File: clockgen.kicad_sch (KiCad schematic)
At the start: 146 parts, among them IC3 TLV74325PDBVR, J13 73391-0083, J14 73391-0083, J15 292161-3, J16 U.FL-R-SMT-180, Q10 BSS138, Q9 BSS138, U12 AZ1117-3.3, U13 AZ1117-3.3, U14 TCA6416APWR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

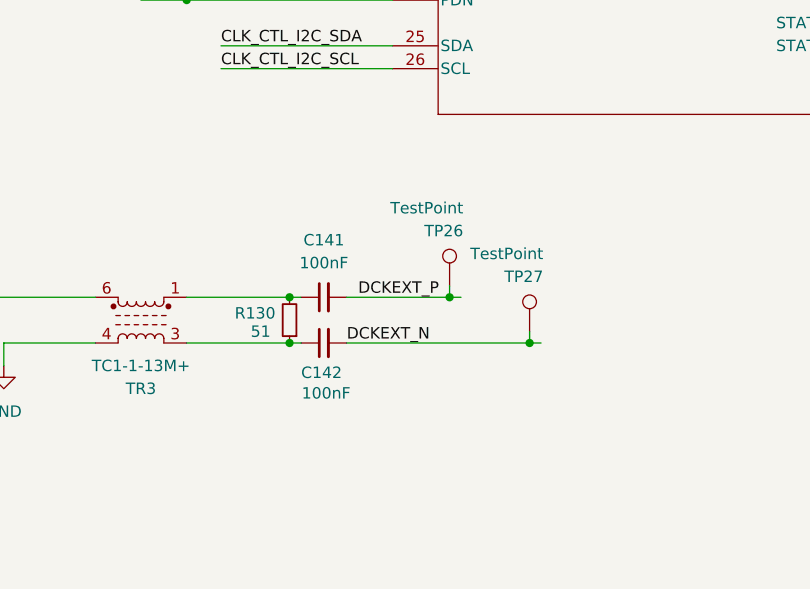
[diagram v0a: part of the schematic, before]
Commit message: schema: external clock input redone
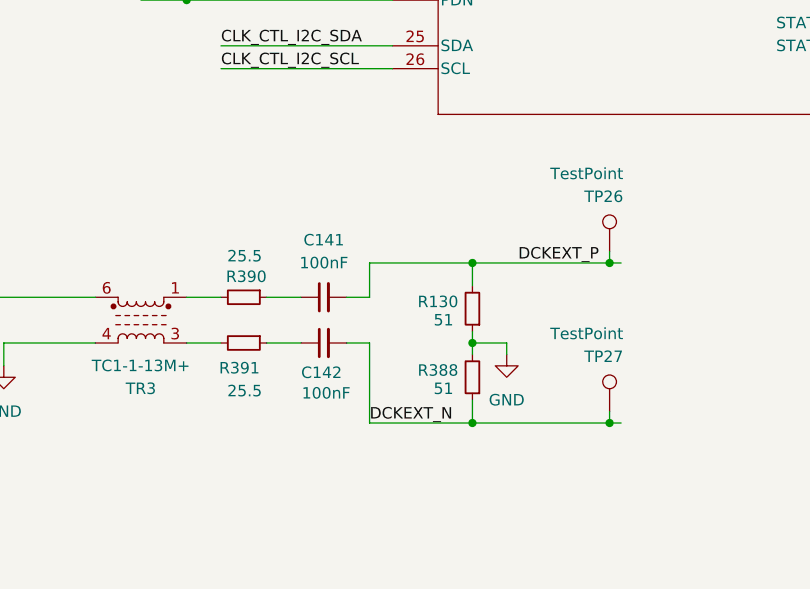
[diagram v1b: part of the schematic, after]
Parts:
- added R388: 51, Resistor_SMD:R_0402_1005Metric, symbol Device:R_Small
- added R390, R391: 25.5, Resistor_SMD:R_0402_1005Metric, symbol Device:R_Small
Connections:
- net DCKEXT_N: now also R388.1
- net DCKEXT_P: now also R130.2
- net GND: now also R130.1, R388.2
- new net: C142.1, R391.1
- new net: R390.2, TR3.1
- new net: R391.2, TR3.3
- new net: C141.1, R390.1
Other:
- moved on the sheet: R130, TP26, TP27

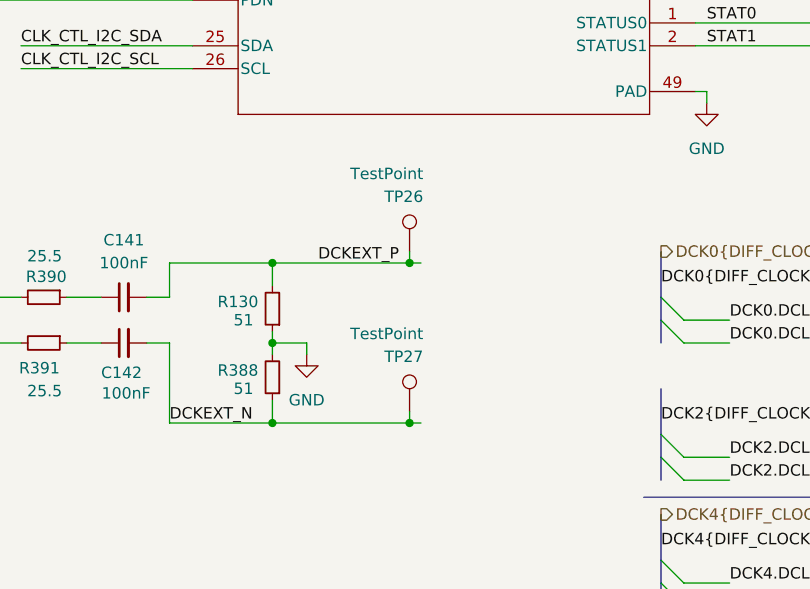
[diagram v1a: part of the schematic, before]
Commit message: ext clock input change
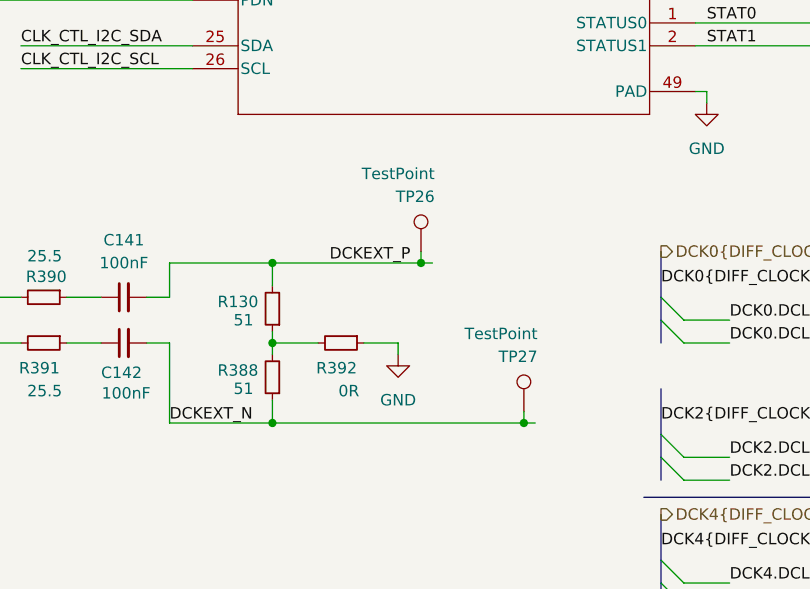
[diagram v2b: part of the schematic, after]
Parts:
- added R392: 0R, Resistor_SMD:R_0603_1608Metric, symbol Device:R_Small
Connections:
- net GND: now also R392.1; no longer R130.1, R388.2
- new net: R130.1, R388.2, R392.2
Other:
- moved on the sheet: TP26, TP27
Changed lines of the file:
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@@
 	(title_block
 		(title "NASR-M")
-		(date "2025-10-21")
-		(rev "D 0.9.4")
+		(date "2025-10-22")
+		(rev "D 0.9.5")
 		(company "electrodyssey.net")
 		(comment 1 "Onboard clock generator with optional external synchronization")
@@
 	)
 	(junction
-		(at 313.69 215.9)
+		(at 326.39 215.9)
 		(diameter 0)
 		(color 0 0 0 0)
@@
 	)
 	(junction
-		(at 313.69 198.12)
+		(at 314.96 198.12)
 		(diameter 0)
 		(color 0 0 0 0)
@@
 	(wire
 		(pts
-			(xy 298.45 215.9) (xy 313.69 215.9)
-		)
-		(stroke
-			(width 0)
-			(type default)
-		)
-	)
-	(wire
-		(pts
 			(xy 38.1 38.1) (xy 49.53 38.1)
 		)
@@
 	(wire
 		(pts
-			(xy 302.26 208.28) (xy 302.26 207.01)
-		)
-		(stroke
-			(width 0)
-			(type default)
-		)
-	)
-	(wire
-		(pts
 			(xy 314.96 43.18) (xy 314.96 41.91)
 		)
@@
 	(wire
 		(pts
-			(xy 313.69 215.9) (xy 314.96 215.9)
+			(xy 326.39 215.9) (xy 327.66 215.9)
 		)
 		(stroke
@@
 	(wire
 		(pts
+			(xy 298.45 215.9) (xy 326.39 215.9)
+		)
+		(stroke
+			(width 0)
+			(type default)
+		)
+	)
+	(wire
+		(pts
 			(xy 193.04 199.39) (xy 195.58 199.39)
 		)
@@
 	(wire
 		(pts
+			(xy 298.45 198.12) (xy 314.96 198.12)
+		)
+		(stroke
+			(width 0)
+			(type default)
+		)
+	)
+	(wire
+		(pts
 			(xy 182.88 240.03) (xy 193.04 240.03)
 		)
@@
 	(wire
 		(pts
-			(xy 313.69 196.85) (xy 313.69 198.12)
+			(xy 314.96 196.85) (xy 314.96 198.12)
 		)
 		(stroke
@@
 	(wire
 		(pts
-			(xy 313.69 198.12) (xy 314.96 198.12)
+			(xy 314.96 198.12) (xy 316.23 198.12)
 		)
 		(stroke
@@
 	(wire
 		(pts
+			(xy 308.61 207.01) (xy 312.42 207.01)
+		)
+		(stroke
+			(width 0)
+			(type default)
+		)
+	)
+	(wire
+		(pts
 			(xy 259.08 73.66) (xy 259.08 72.39)
 		)
@@
 	(wire
 		(pts
-			(xy 302.26 207.01) (xy 298.45 207.01)
+			(xy 298.45 207.01) (xy 303.53 207.01)
 		)
 		(stroke
@@
 	(wire
 		(pts
-			(xy 298.45 198.12) (xy 313.69 198.12)
-		)
-		(stroke
-			(width 0)
-			(type default)
-		)
-	)
-	(wire
-		(pts
 			(xy 212.09 266.7) (xy 212.09 267.97)
 		)
@@
 	(wire
 		(pts
-			(xy 313.69 214.63) (xy 313.69 215.9)
+			(xy 326.39 214.63) (xy 326.39 215.9)
 		)
 		(stroke
@@
 	(wire
 		(pts
+			(xy 312.42 208.28) (xy 312.42 207.01)
+		)
+		(stroke
+			(width 0)
+			(type default)
+		)
+	)
+	(wire
+		(pts
 			(xy 201.93 261.62) (xy 201.93 267.97)
 		)
@@
 	)
 	(label "DCKEXT_P"
-		(at 303.53 198.12 0)
+		(at 304.8 198.12 0)
 		(effects
 			(font
@@
 	(symbol
 		(lib_id "Connector:TestPoint")
-		(at 313.69 196.85 0)
+		(at 314.96 196.85 0)
 		(unit 1)
 		(exclude_from_sim no)
@@
 		(dnp no)
 		(property "Reference" "TP26"
-			(at 315.214 190.754 0)
+			(at 316.484 190.754 0)
 			(effects
 				(font
@@
 		)
 		(property "Value" "TestPoint"
-			(at 315.214 188.214 0)
+			(at 316.484 188.214 0)
 			(effects
 				(font
@@
 		)
 		(property "Footprint" "TestPoint:TestPoint_Pad_D1.0mm"
-			(at 318.77 196.85 0)
+			(at 320.04 196.85 0)
 			(effects
 				(font
@@
 		)
 		(property "Datasheet" "~"
-			(at 318.77 196.85 0)
+			(at 320.04 196.85 0)
 			(effects
 				(font
@@
 		)
 		(property "Description" "test point"
-			(at 313.69 196.85 0)
+			(at 314.96 196.85 0)
 			(effects
 				(font
@@
 		)
 		(property "Mouser " ""
-			(at 313.69 196.85 0)
+			(at 314.96 196.85 0)
 			(effects
 				(font
@@
 	(symbol
 		(lib_id "power:GND")
-		(at 302.26 208.28 0)
+		(at 312.42 208.28 0)
 		(unit 1)
 		(exclude_from_sim no)
@@
 		(fields_autoplaced yes)
 		(property "Reference" "#PWR060"
-			(at 302.26 214.63 0)
+			(at 312.42 214.63 0)
 			(effects
 				(font
@@
 		)
 		(property "Value" "GND"
-			(at 302.26 213.36 0)
+			(at 312.42 213.36 0)
 			(effects
 				(font
@@
 		)
 		(property "Footprint" ""
-			(at 302.26 208.28 0)
+			(at 312.42 208.28 0)
 			(effects
 				(font
@@
 		)
 		(property "Datasheet" ""
-			(at 302.26 208.28 0)
+			(at 312.42 208.28 0)
 			(effects
 				(font
@@
 		)
 		(property "Description" "Power symbol creates a global label with name \"GND\" , ground"
-			(at 302.26 208.28 0)
+			(at 312.42 208.28 0)
 			(effects
 				(font
@@
 	)
 	(symbol
+		(lib_id "Device:R_Small")
+		(at 306.07 207.01 270)
+		(unit 1)
+		(exclude_from_sim no)
+		(in_bom yes)
+		(on_board yes)
+		(dnp no)
+		(property "Reference" "R392"
+			(at 307.848 209.804 90)
+			(effects
+				(font
+					(size 1.27 1.27)
+				)
+				(justify right)
+			)
+		)
+		(property "Value" "0R"
+			(at 308.102 212.344 90)
+			(effects
+				(font
+					(size 1.27 1.27)
+				)
+				(justify right)
+			)
+		)
+		(property "Footprint" "Resistor_SMD:R_0603_1608Metric"
+			(at 306.07 207.01 0)
+			(effects
+				(font
+					(size 1.27 1.27)
+				)
+				(hide yes)
+			)
+		)
+		(property "Datasheet" "~"
+			(at 306.07 207.01 0)
+			(effects
+				(font
+					(size 1.27 1.27)
+				)
+				(hide yes)
+			)
+		)
+		(property "Description" ""
+			(at 306.07 207.01 0)
+			(effects
+				(font
+					(size 1.27 1.27)
+				)
+				(hide yes)
+			)
+		)
+		(property "JLCPCB Part #" "C2906974"
+			(at 306.07 207.01 0)
+			(effects
+				(font
+					(size 1.27 1.27)
+				)
+				(hide yes)
+			)
+		)
+		(property "Part" "FRC0603F0000TS"
+			(at 306.07 207.01 90)
+			(effects
+				(font
+					(size 1.27 1.27)
+				)
+				(hide yes)
+			)
+		)
+		(property "Mouser " ""
+			(at 306.07 207.01 90)
+			(effects
+				(font
+					(size 1.27 1.27)
+				)
+				(hide yes)
+			)
+		)
+		(pin "1"
+		)
+		(pin "2"
+		)
+		(instances
+			(project "NASR"
+				(path "/9a13c8f9-b8a2-41aa-b5bd-813f44236e01/9e585404-97af-4e2a-aa37-2875da9a13db"
+					(reference "R392")
+					(unit 1)
+				)
+			)
+		)
+	)
+	(symbol
 		(lib_id "Device:C_Small")
 		(at 252.73 104.14 180)
@@
 	(symbol
 		(lib_id "Connector:TestPoint")
-		(at 313.69 214.63 0)
+		(at 326.39 214.63 0)
 		(unit 1)
 		(exclude_from_sim no)
@@
 		(dnp no)
 		(property "Reference" "TP27"
-			(at 315.214 208.534 0)
+			(at 327.914 208.534 0)
 			(effects
 				(font
@@
 		)
 		(property "Value" "TestPoint"
-			(at 315.214 205.994 0)
+			(at 327.914 205.994 0)
 			(effects
 				(font
@@
 		)
 		(property "Footprint" "TestPoint:TestPoint_Pad_D1.0mm"
-			(at 318.77 214.63 0)
+			(at 331.47 214.63 0)
 			(effects
 				(font
@@
 		)
 		(property "Datasheet" "~"
-			(at 318.77 214.63 0)
+			(at 331.47 214.63 0)
 			(effects
 				(font
@@
 		)
 		(property "Description" "test point"
-			(at 313.69 214.63 0)
+			(at 326.39 214.63 0)
 			(effects
 				(font
@@
 		)
 		(property "Mouser " ""
-			(at 313.69 214.63 0)
+			(at 326.39 214.63 0)
 			(effects
 				(font
